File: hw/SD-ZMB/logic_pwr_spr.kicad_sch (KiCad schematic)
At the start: 83 parts

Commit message: ZMB: Diagrams and start of PCB. DBG: Updated WAIT. DADPT: Display/Cable PCB ordered.
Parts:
- removed C1, C2, C3, C5, C7: 0.1uF, symbol Device:C_Small
- removed J?: HDR 2x3, symbol Connector_Generic:Conn_02x03_Row_Letter_First
- removed J?: HDR 1x2, symbol Connector_Generic:Conn_01x02
- removed SW?: SW_DIP_x03, symbol Switch:SW_DIP_x03
- removed U? (x6): 74HCT32, symbol 74xx:74LS32
- removed U? (x3): 74HCT08, symbol 74xx:74LS08
- removed U? (x9): 74HCT00, symbol 74xx:74HC00
- removed U? (x7): 74AHC08, symbol 74xx:74LS08
- removed U? (x4): 74HC04, symbol AES_Library:7404-AES
- removed U?: 74HC00, symbol 74xx:74HC00
- removed U? (x2): 74AHC32, symbol 74xx:74LS32
- removed U?: 74HCT14, symbol AES_Library:74HC14-AES
- removed U? (x3): 74LS08, symbol 74xx:74LS08
- removed U? (x4): 74HC02, symbol 74xx:74HC02
- removed U?: 74HCT74, symbol 74xx:74HC74
- removed U?: 74HCT11, symbol 74xx:74LS11
- removed U?: 74AHC244, symbol 74xx:74AHCT244
- removed U? (x5): 74HCT86, symbol 74xx:74LS86
- removed U? (x2): 74HCT02, symbol 74xx:74HC02
- removed U? (x2): 74LS11, symbol 74xx:74LS11
- removed U?: 74HCT393, symbol 74xx:74LS393
- removed U?: 74HCT74, symbol 74xx:74HCT74
- removed U? (x2): 74HC4002, symbol 4xxx:4002
- added C10, C11, C15, C16, C17, C18, C19, C20, C21, C22, C23, C24, C25, C26, C32, C33, C35, C36, C37, C38, C39, C40, C9: 0.1uF, Capacitor_SMD:C_0603_1608Metric_Pad1.08x0.95mm_HandSolder, symbol Device:C_Small
- added C? (x2): 330.0pF, Capacitor_SMD:C_0603_1608Metric_Pad1.08x0.95mm_HandSolder, symbol Device:C_Small
- added D? (x2): BAS7002VH6327XTSA1, symbol Device:D_Schottky_Small_Filled
- added H1, H2, H3, H4: MountingHole, MountingHole:MountingHole_3.2mm_M3, symbol Mechanical:MountingHole
- added H5, H6, H7: MountingHole, MountingHole:MountingHole_2.7mm_M2.5, symbol Mechanical:MountingHole
- added J? (x2): Conn_02x02_Row_Letter_First, symbol Connector_Generic:Conn_02x02_Row_Letter_First
- added J?: Conn_02x05_Row_Letter_First, symbol Connector_Generic:Conn_02x05_Row_Letter_First
- added J?: HDR 02x02, AES_Library:PinHeader_2x02_AB-AES, symbol Connector_Generic:Conn_02x02_Row_Letter_First
- added R? (x2): 27.4, Resistor_SMD:R_0805_2012Metric_Pad1.20x1.40mm_HandSolder, symbol Device:R_Small_US
- added R? (x2): 22, Resistor_SMD:R_0805_2012Metric_Pad1.20x1.40mm_HandSolder, symbol Device:R_Small_US
- added U10, U?: 74F260, Package_SO:SOIC-14_3.9x8.7mm_P1.27mm, symbol AES_Library:74F260-AES
- added U14, U29: 74F27, Package_SO:SOIC-14_3.9x8.7mm_P1.27mm, symbol 74xx:74LS27
- added U19, U34: 74AHCT10, Package_SO:SOIC-14_3.9x8.7mm_P1.27mm, symbol 74xx:74LS10
- added unit 3 of U20
- added unit 2 of U20
- added U38, U?: 74AHCT32, Package_SO:SOIC-14_3.9x8.7mm_P1.27mm, symbol 74xx:74LS32
- added U5: 74AHCT08, Package_SO:SOIC-14_3.9x8.7mm_P1.27mm, symbol 74xx:74LS08
- added U6: 74AHCT00, Package_SO:SOIC-14_3.9x8.7mm_P1.27mm, symbol 74xx:74HC00
- added U? (x6): 74AHCT08, symbol 74xx:74LS08
- added U? (x2): 74AHCT164, symbol 74xx:74HC164
- added U? (x5): 74AHCT32, symbol 74xx:74LS32
- added U? (x3): 74LV21, symbol 74xx:74LS21
- added U? (x5): 74LVC125, symbol 74xx:74LVC125
- added U? (x3): 74AHCT74DR, Package_SO:SOIC-14_3.9x8.7mm_P1.27mm, symbol 74xx:74HC74
- added U? (x8): 74AHCT04, symbol AES_Library:7404-AES
- added U?: 74AHCT02, Package_SO:SOIC-14_3.9x8.7mm_P1.27mm, symbol 74xx:74HC02
- C12, C13, C14, C27, C28, C29, C30, C31, C34, C8: footprint (none) -> Capacitor_SMD:C_0603_1608Metric_Pad1.08x0.95mm_HandSolder
- C7: renamed from C26; footprint (none) -> Capacitor_SMD:C_0603_1608Metric_Pad1.08x0.95mm_HandSolder
- U11, U32: renamed from U?; value 74HCT74 -> 74AHCT74DR; footprint (none) -> Package_SO:SOIC-14_3.9x8.7mm_P1.27mm
- U2: renamed from U?; value 74HC74 -> 74AHCT74DR; footprint (none) -> Package_SO:SOIC-14_3.9x8.7mm_P1.27mm
- U20: renamed from U?; value 74HCT11 -> 74AC11; footprint (none) -> Package_SO:SOIC-14_3.9x8.7mm_P1.27mm
- U4: renamed from U?; value 74HCT08 -> 74AHCT08; footprint (none) -> Package_SO:SOIC-14_3.9x8.7mm_P1.27mm; PropDly (none) -> (9nS)
- U7: renamed from U?; value 74HC02 -> 74AHCT02; footprint (none) -> Package_SO:SOIC-14_3.9x8.7mm_P1.27mm; PropDly (none) -> (9nS)
- U8: renamed from U?; value 74HC00 -> 74AHCT00; footprint (none) -> Package_SO:SOIC-14_3.9x8.7mm_P1.27mm
- U9: renamed from U?; value 74HCT32 -> 74AHCT32; footprint (none) -> Package_SO:SOIC-14_3.9x8.7mm_P1.27mm; PropDly (none) -> (10nS)
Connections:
- net GND is gone; now on net +5V: C12.1, C13.1, C14.1, C27.1, C28.1, C29.1, C30.1, C31.1, C34.1, C7.1, C8.1, U11.7 (GND), U20.7 (GND), U32.7 (GND), U4.7 (GND), U9.7 (GND)
- net +5V: now also C12.2, C13.2, C14.2, C8.2, U2.14 (VCC), U2.7 (GND), U7.14 (VCC), U7.7 (GND), U8.14 (VCC), U8.7 (GND), C10.1, C10.2, C11.1, C11.2, C15.1, C15.2, C16.1, C16.2, C17.1, C17.2, C18.1, C18.2, C19.1, C19.2, C20.1, C20.2, C21.1, C21.2, C22.1, C22.2, C23.1, C23.2, C24.1, C24.2, C25.1, C25.2, C26.1, C26.2, C32.1, C32.2, C33.1, C33.2, C35.1, C35.2, C36.1, C36.2, C37.1, C37.2, C38.1, C38.2, C39.1, C39.2, C40.1, C40.2, C9.1, C9.2, C?.2, C?.2, J?.a1 (Pin_a1), U10.14 (VCC), U10.7 (GND), U14.14 (VCC), U14.7 (GND), U19.14 (VCC), U19.7 (GND), U20.10, U20.11, U20.3, U20.4, U20.5, U20.9, U29.14 (VCC), U29.7 (GND), U34.14 (VCC), U34.7 (GND), U38.10, U38.14 (VCC), U38.7 (GND), U38.9, U5.14 (VCC), U5.7 (GND), U6.14 (VCC), U6.7 (GND), U?.12 (D), U?.12 (D), U?.2 (D)
- net ZCLK: now also R?.2, R?.2, U?.8 (CP), U?.8 (CP)
- net ZINT-: now also U?.9
- net ZIORQ-: now also U?.10, U?.3, U?.3, U?.5, U?.5
- net ZM1-: now also J?.a2 (Pin_a2), U?.10
- net ZRST-: now also U?.1
- new net: U?.1, U?.6
- new net: U?.2, U?.3
- new net: U?.1 (DSA), U?.2 (DSB), U?.4, U?.9 (~{MR})
- new net: J?.a1 (Pin_a1), U?.4 (Q1)
- new net: J?.a2 (Pin_a2), U?.5 (Q2)
- new net: J?.b1 (Pin_b1), J?.b2 (Pin_b2), J?.b3 (Pin_b3), J?.b4 (Pin_b4), J?.b5 (Pin_b5), U?.9
- new net: C?.1, D?.2 (A), R?.2, U?.1
- new net: J?.a2 (Pin_a2), U?.4 (Q1)
- new net: J?.a3 (Pin_a3), U?.5 (Q2)
- new net: J?.a4 (Pin_a4), U?.6 (Q3)
- new net: J?.a5 (Pin_a5), U?.10 (Q4)
- new net: R?.1, U?.3
- new net: U?.13, U?.2, U?.4
- new net: U?.12, U?.6
- new net: R?.1, U?.6
- new net: U?.1, U?.13
- new net: J?.b1 (Pin_b1), J?.b2 (Pin_b2), U?.5
- new net: C?.1, D?.2 (A), R?.2, U?.4
- new net: J?.b1 (Pin_b1), J?.b2 (Pin_b2), U?.1, U?.1 (~{R})
- new net: U?.11, U?.4 (~{S})
- new net: U?.10 (~{S}), U?.6
- new net: J?.a2 (Pin_a2), U?.3
- new net B1IEO: U?.4
- new net CLK: U?.2, U?.2, U?.5, U?.8
- new net CLK-: U?.11 (C)
- new net CLK2: U?.1, U?.2
- new net CLK2EN-: D?.1 (K), R?.1, U?.4, U?.9 (Q)
- new net CLK2RST-: U?.8 (~{Q})
- new net CLK2SW: U?.11, U?.11 (C), U?.5
- new net CLKEN-: D?.1 (K), R?.1, U?.12, U?.8 (~{Q})
- new net CLKSET-: U?.10 (~{S}), U?.5 (Q)
- new net CLKSW: U?.3 (C), U?.6
- new net FSCLK-: U?.2
- new net IAM1: U?.1 (DSA), U?.2, U?.4, U?.9 (~{MR})
- new net IAM1-: J?.b1 (Pin_b1), J?.b2 (Pin_b2), U?.1, U?.1
- new net IORQD-: U?.2, U?.6
- new net IOWAIT-: U?.8
- new net PIORQ-: U?.3
- new net VP: J?.a1 (Pin_a1), J?.a1 (Pin_a1), U?.13 (~{R}), U?.13 (~{R}), U?.2 (DSB)
- new net ZMREQ: U?.11, U?.8
- new net ZMREQ-: U?.9
- no-connect marks 0 -> 6
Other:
- moved on the sheet: C7, U11C, U20D, U2C, U32C, U4E, U7E, U8E, U9E

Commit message: ZMB: v1.0 Board RFP
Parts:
- removed C36, C37, C38, C39: 0.1uF, Capacitor_SMD:C_0603_1608Metric_Pad1.08x0.95mm_HandSolder, symbol Device:C_Small
- removed C? (x2): 330.0pF, Capacitor_SMD:C_0603_1608Metric_Pad1.08x0.95mm_HandSolder, symbol Device:C_Small
- removed D? (x2): BAS7002VH6327XTSA1, symbol Device:D_Schottky_Small_Filled
- removed J? (x2): Conn_02x02_Row_Letter_First, symbol Connector_Generic:Conn_02x02_Row_Letter_First
- removed J?: Conn_02x05_Row_Letter_First, symbol Connector_Generic:Conn_02x05_Row_Letter_First
- removed J?: HDR 02x02, AES_Library:PinHeader_2x02_AB-AES, symbol Connector_Generic:Conn_02x02_Row_Letter_First
- removed R? (x2): 27.4, Resistor_SMD:R_0805_2012Metric_Pad1.20x1.40mm_HandSolder, symbol Device:R_Small_US
- removed R? (x2): 22, Resistor_SMD:R_0805_2012Metric_Pad1.20x1.40mm_HandSolder, symbol Device:R_Small_US
- removed unit 2 of U20
- removed unit 3 of U38
- removed U? (x6): 74AHCT08, symbol 74xx:74LS08
- removed U? (x2): 74AHCT164, symbol 74xx:74HC164
- removed U? (x5): 74AHCT32, symbol 74xx:74LS32
- removed U? (x2): 74LV21, symbol 74xx:74LS21
- removed U? (x3): 74AHCT74DR, Package_SO:SOIC-14_3.9x8.7mm_P1.27mm, symbol 74xx:74HC74
- removed U?: 74F260, Package_SO:SOIC-14_3.9x8.7mm_P1.27mm, symbol AES_Library:74F260-AES
- removed U? (x7): 74AHCT04, symbol AES_Library:7404-AES
- removed U?: 74AHCT02, Package_SO:SOIC-14_3.9x8.7mm_P1.27mm, symbol 74xx:74HC02
- removed U?: 74AHCT32, Package_SO:SOIC-14_3.9x8.7mm_P1.27mm, symbol 74xx:74LS32
- removed U? (x2): 74LVC125, symbol 74xx:74LVC125
- added unit 2 of U41
- added U42: 74F260, Package_SO:SOIC-14_3.9x8.7mm_P1.27mm, symbol AES_Library:74F260-AES
- C10, C11, C12, C13, C14, C15, C16, C17, C18, C19, C20, C21, C22, C23, C24, C25, C26, C27, C28, C29, C30, C31, C32, C33, C34, C35, C40, C7, C8, C9: footprint Capacitor_SMD:C_0603_1608Metric_Pad1.08x0.95mm_HandSolder -> Capacitor_SMD:C_0603_1608Metric
- U11, U2, U32: value 74AHCT74DR -> 74AHCT74
- U19, U34: value 74AHCT10 -> 74ACT10
- U20: value 74AC11 -> 74ACT11; PropDly (none) -> (9nS)
- U20: value 74AC11 -> 74ACT11; PropDly (10nS) -> (9nS)
- U39, U41: renamed from U?; footprint (none) -> Package_SO:SOIC-14_3.9x8.7mm_P1.27mm
- U44: renamed from U?; value 74LVC125 -> 74LVC125AS; footprint (none) -> Package_SO:SOIC-14_3.9x8.7mm_P1.27mm; Function 5-3V -> (none)
- U44: renamed from U?; value 74LVC125 -> 74LVC125AS; footprint (none) -> Package_SO:SOIC-14_3.9x8.7mm_P1.27mm
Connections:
- net +5V: now also U39.14 (VCC), U41.14 (VCC), U44.14 (VCC), U42.14 (VCC); no longer C10.1, C11.1, C12.1, C13.1, C14.1, C15.1, C16.1, C17.1, C18.1, C19.1, C20.1, C21.1, C22.1, C23.1, C24.1, C25.1, C26.1, C27.1, C28.1, C29.1, C30.1, C31.1, C32.1, C33.1, C34.1, C35.1, C40.1, C7.1, C8.1, C9.1, U10.7 (GND), U11.7 (GND), U14.7 (GND), U19.7 (GND), U2.7 (GND), U20.10, U20.11, U20.7 (GND), U20.9, U29.7 (GND), U32.7 (GND), U34.7 (GND), U38.7 (GND), U4.7 (GND), U5.7 (GND), U6.7 (GND), U7.7 (GND), U8.7 (GND), U9.7 (GND)
- net GND: now reaches U44.12
- net GND: now also C10.1, C11.1, C12.1, C13.1, C14.1, C15.1, C16.1, C17.1, C18.1, C19.1, C20.1, C21.1, C22.1, C23.1, C24.1, C25.1, C26.1, C27.1, C28.1, C29.1, C30.1, C31.1, C32.1, C33.1, C34.1, C35.1, C40.1, C7.1, C8.1, C9.1, U10.7 (GND), U11.7 (GND), U14.7 (GND), U19.7 (GND), U2.7 (GND), U20.10, U20.11, U20.7 (GND), U20.9, U29.7 (GND), U32.7 (GND), U34.7 (GND), U38.7 (GND), U39.7 (GND), U4.7 (GND), U41.7 (GND), U44.7 (GND), U44.9, U5.7 (GND), U6.7 (GND), U7.7 (GND), U8.7 (GND), U9.7 (GND), U41.10, U41.12, U41.13, U41.9, U42.7 (GND)
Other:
- moved on the sheet: C10, C11, C12, C13, C14, C15, C16, C17, C18, C19, C20, C21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

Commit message: PCB received
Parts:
- added SPARE1: ~, AES_Library:SPARE-and-SOIC-16-AES, symbol AES_Library:SPARE-16-AES
- added SPARE2, SPARE3: ~, AES_Library:SPARE-16-SOT-5_6-AES, symbol AES_Library:SPARE-16-AES
- renumbered U7 to U13, U5 to U15, U9 to U16, U4 to U17, U29 to U20, U6 to U27, U8 to U28, U11 to U29, U32 to U35, U2 to U38, U38 to U39, U10 to U4, U42 to U40, U39 to U41, U41 to U45, U20 to U46, U34 to U7

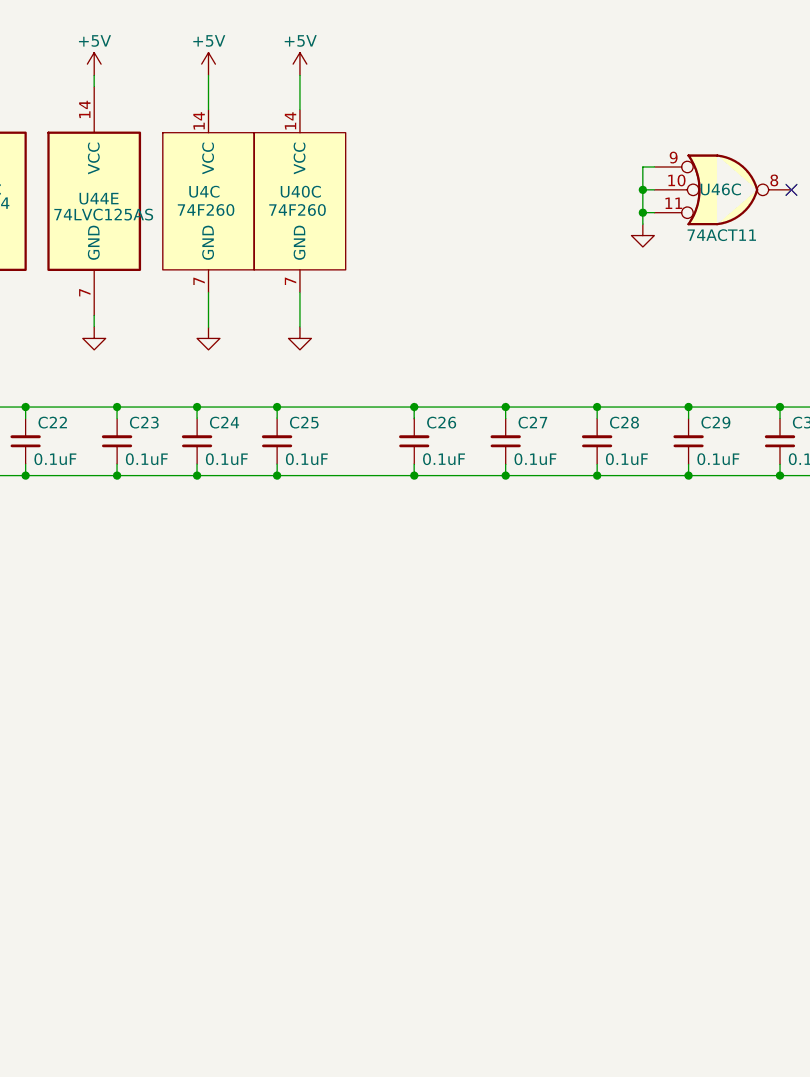
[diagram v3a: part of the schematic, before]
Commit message: ECO.A: PG Reg A3 incorrect. Change U17B AND to SPR.1A OR
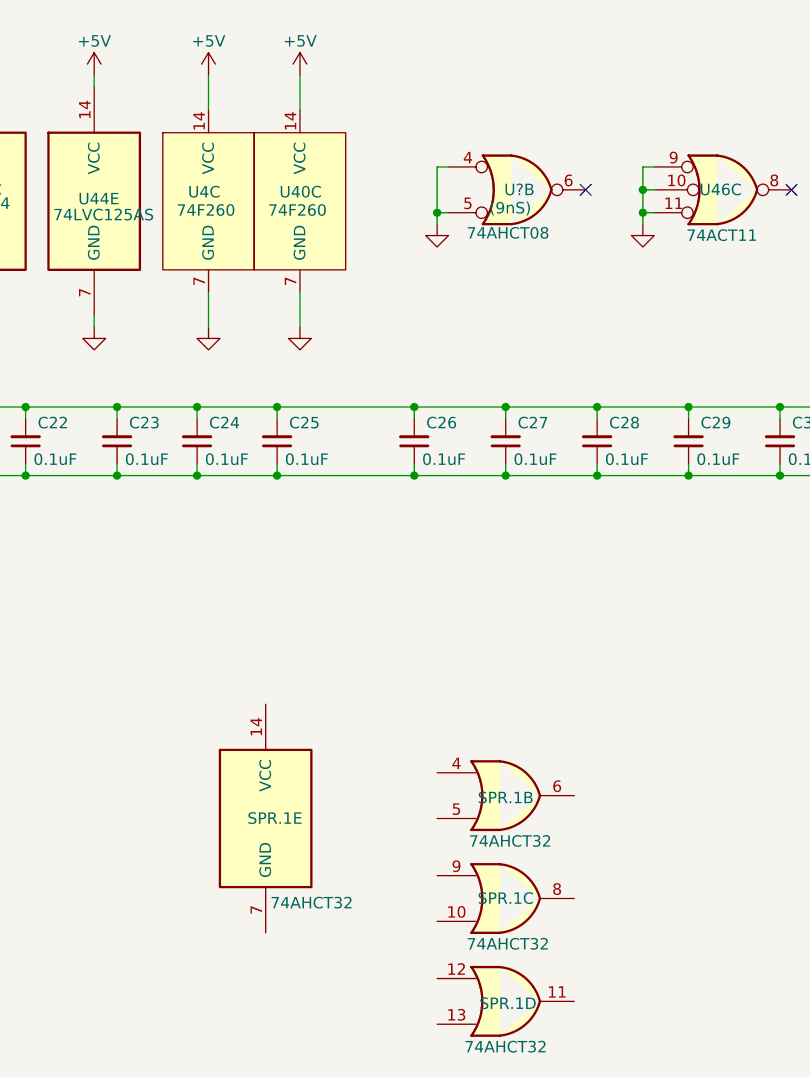
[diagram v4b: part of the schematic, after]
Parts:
- added SPR.1: 74AHCT32, symbol 74xx:74LS32
- added U?: 74AHCT08, Package_SO:SOIC-14_3.9x8.7mm_P1.27mm, symbol 74xx:74LS08
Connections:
- net GND: now also U?.4, U?.5
- no-connect marks 6 -> 7
